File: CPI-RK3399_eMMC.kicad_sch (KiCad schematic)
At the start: 1 part, among them U1 RK3399

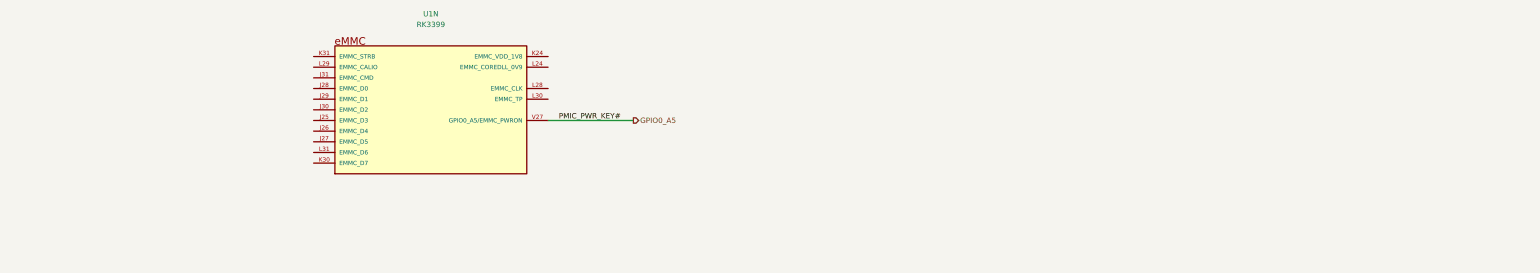
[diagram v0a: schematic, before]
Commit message: design CPU-RK3399 eMMC Controller
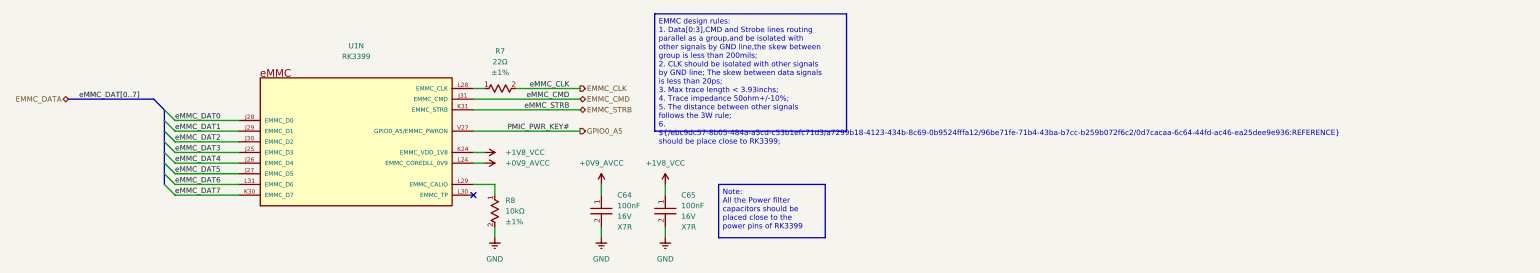
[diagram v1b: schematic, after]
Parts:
- added C64, C65: ~, footprints:CAPC1005X50N, symbol component_library:Capacitors/CL05B104KO5NNNC
- added R7: ~, footprints:RESC1005X35N, symbol component_library:Resistors/0402WGF220JTCE
- added R8: ~, footprints:RESC1005X35N, symbol component_library:Resistors/0402WGF1002TCE
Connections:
- net eMMC_DAT3: now reaches U1.J25 (EMMC_D3)
- net eMMC_DAT4: now reaches U1.J26 (EMMC_D4)
- net eMMC_DAT5: now reaches U1.J27 (EMMC_D5)
- net eMMC_DAT0: now reaches U1.J28 (EMMC_D0)
- net eMMC_DAT1: now reaches U1.J29 (EMMC_D1)
- net eMMC_DAT2: now reaches U1.J30 (EMMC_D2)
- net EMMC_CMD: now reaches U1.J31 (EMMC_CMD)
- net +1V8_VCC: now reaches U1.K24 (EMMC_VDD_1V8)
- net +1V8_VCC: now also C65.1
- net eMMC_DAT7: now reaches U1.K30 (EMMC_D7)
- net EMMC_STRB: now reaches U1.K31 (EMMC_STRB)
- net +0V9_AVCC: now reaches U1.L24 (EMMC_COREDLL_0V9)
- net +0V9_AVCC: now also C64.1
- net at U1.L28 (EMMC_CLK): now also R7.1
- net at U1.L29 (EMMC_CALIO): now also R8.1
- net eMMC_DAT6: now reaches U1.L31 (EMMC_D6)
- new net EMMC_CLK: R7.2
- new net GND: C64.2, C65.2, R8.2
- no-connect marks 0 -> 1
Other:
- company: (none) -> TickLab
- moved on the sheet: U1N
